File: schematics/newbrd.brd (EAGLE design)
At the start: 45 x 45 mm, 37 parts, among them IC1 TLC271D, IC2 TLC271D

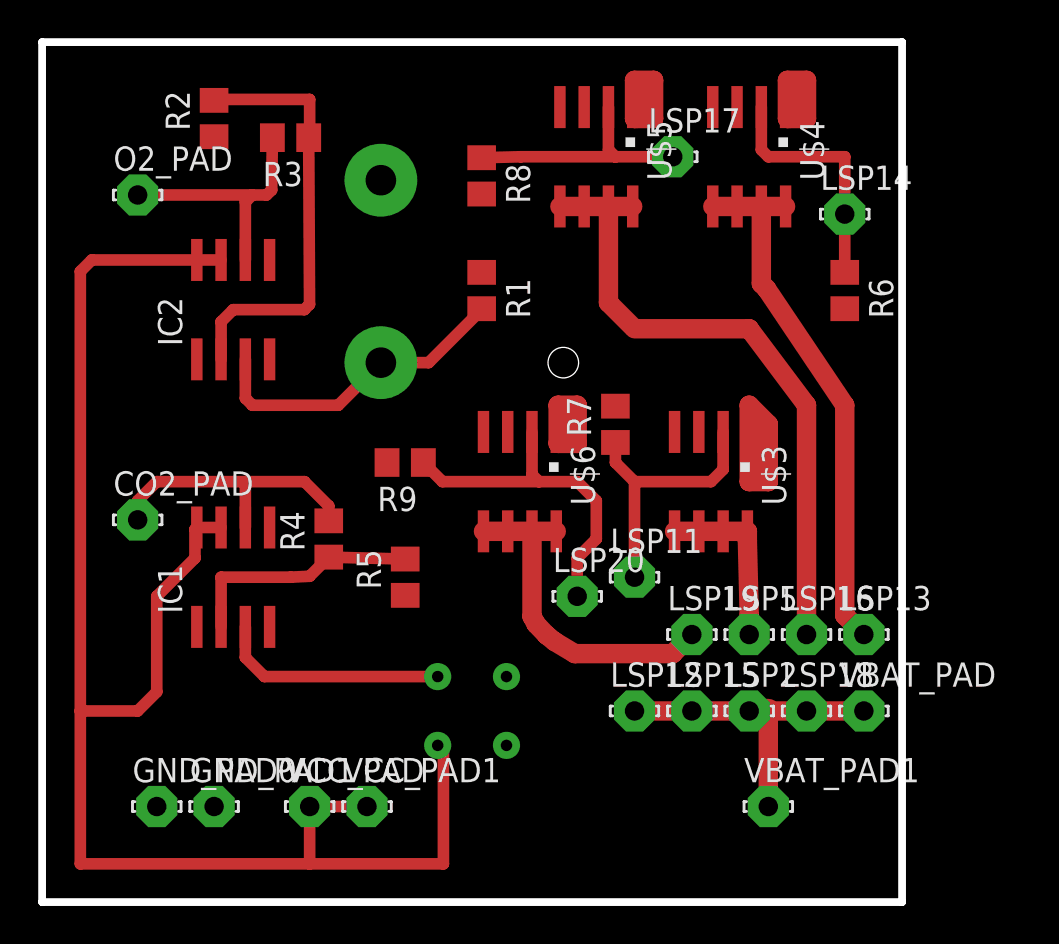
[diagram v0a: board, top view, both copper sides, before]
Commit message: Правки платы для аналоговых устройств и доделана плата для I2C устройств
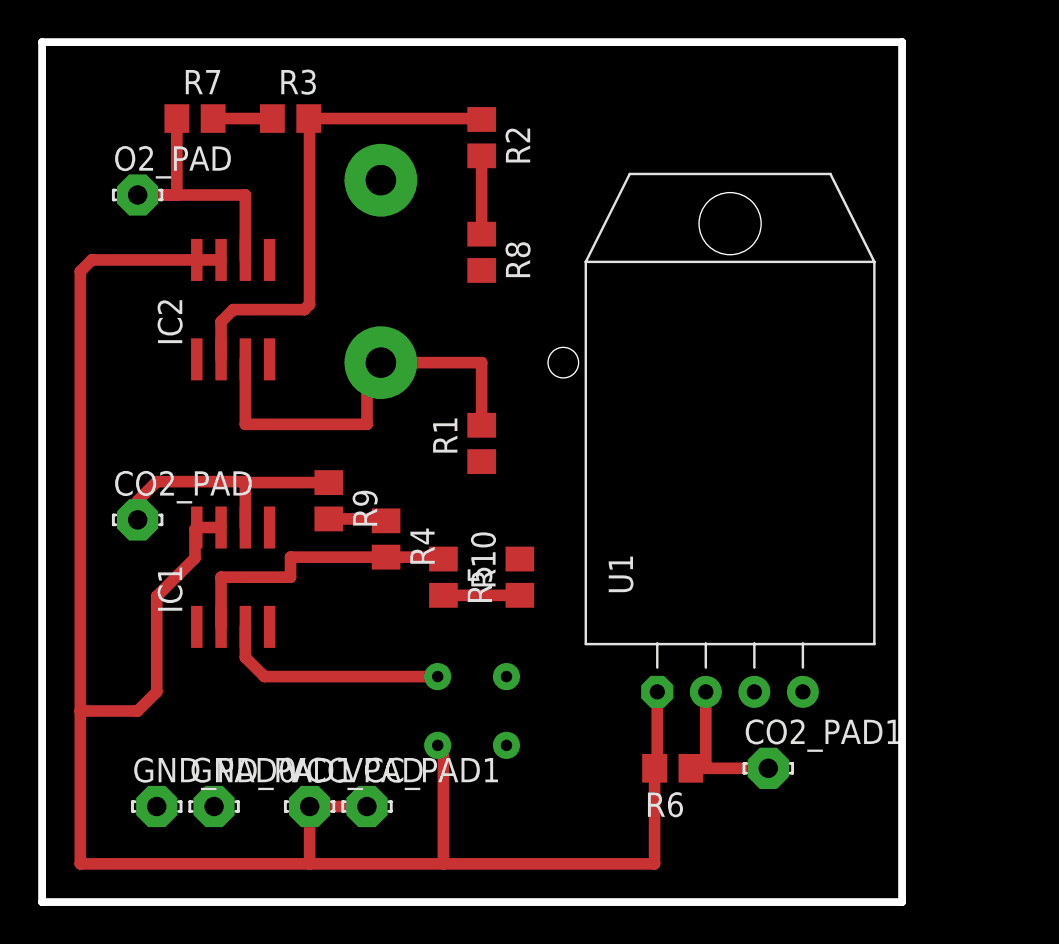
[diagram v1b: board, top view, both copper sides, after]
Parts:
- removed LSP11, LSP12, LSP13, LSP14, LSP15, LSP16, LSP17, LSP18, LSP19, LSP2, LSP20, LSP5, VBAT_PAD, VBAT_PAD1: LSP10, solpad:LSP10
- removed U$3, U$4, U$5, U$6: AO4606, elements:SOIC-8
- added CO2_PAD1: LSP10, solpad:LSP10
- added R10: (no value), resistor:R0805
- added U1: (no value), RHT03_DHT-22_AM2302:RHT03_DHT-22/RA
- moved R7 27.2 mm to (8.00, 41.0), turned to 0 degrees
- moved R6 26.6 mm to (33.0, 7.00), turned to 180 degrees
- moved R2 14.0 mm to (23.0, 40.0), turned to 270 degrees
- moved R1 8.00 mm to (23.0, 24.0), turned to 90 degrees
- moved R9 4.47 mm to (15.0, 21.0), turned to 270 degrees
- moved R8 4.00 mm to (23.0, 34.0)
- moved R4 3.00 mm to (18.0, 19.0), turned to 270 degrees
- moved R5 2.00 mm to (21.0, 17.0), turned to 270 degrees
- moved R3 1.00 mm to (13.0, 41.0), turned to 0 degrees
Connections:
- removed net N$12: LSP13.MP, U$4.5, U$4.6, U$4.7, U$4.8
- removed net N$15: LSP16.MP, U$5.5, U$5.6, U$5.7, U$5.8
- removed net N$16: LSP17.MP, R8.1, U$5.2
- removed net N$18: LSP19.MP, U$6.5, U$6.6, U$6.7, U$6.8
- removed net N$19: LSP20.MP, R9.1, U$6.2
- removed net N$9: IC1.2, R4.1, R5.2
- new net N$11: R10.1, R5.2
- new net N$2: CO2_PAD1.MP, R6.1, U1.DATA
- net GND: now also R10.2, U1.GND; no longer R2.1, R5.1, R6.2, R7.2, R9.2, U$3.1, U$4.1, U$5.1, U$6.1
- net N$10: now also R4.1, R9.2; no longer LSP11.MP, R7.1, U$3.2
- net N$13: now also IC1.2, R4.2, R5.1; no longer LSP14.MP, R6.1, U$4.2
- net N$3: now also R2.1, R3.2; no longer R2.2, R3.1
- net N$4: now also R7.1; no longer R3.2
- net N$6: now also R9.1; no longer R4.2
- net N$7: now also R3.1, R7.2; no longer LSP12.MP, LSP15.MP, LSP18.MP, LSP2.MP, VBAT_PAD.MP, VBAT_PAD1.MP
- net N$8: now also R2.2, R8.1; no longer LSP5.MP, U$3.5, U$3.6, U$3.7, U$3.8
- net VCC: now also R6.2, U1.VDD
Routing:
- net N$15: track 33.6 -> 0.00 mm
- net N$12: track 28.0 -> 0.00 mm
- net GND: track 27.4 -> 0.00 mm
- net VCC: track 85.3 -> 105.5 mm
- net N$19: track 18.0 -> 0.00 mm
- net N$18: track 17.8 -> 0.00 mm
- net N$7: track 17.0 -> 3.10 mm
- net N$16: track 12.8 -> 0.00 mm
- net N$9: track 12.7 -> 0.00 mm
- net N$10: track 14.3 -> 3.10 mm
- net N$2: track 0.00 -> 8.05 mm
- net N$1: track 16.7 -> 22.3 mm
- net N$8: track 9.21 -> 4.10 mm
- net N$11: track 0.00 -> 4.00 mm
- net N$3: track 22.8 -> 25.8 mm
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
